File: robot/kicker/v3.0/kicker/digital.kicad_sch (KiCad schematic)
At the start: 46 parts, among them J12 Conn_01x02, J2 Conn_ARM_JTAG_SWD_10, J4 Conn_01x10, Q4 BSS138K, SW1 BTN0, SW1 RST, SW4 SW_DIP_x04, U12 AT25DF041x-UxN-x, U13 AD8494, U4 STM32F411RETx, U5 SK9822, U6 SK9822

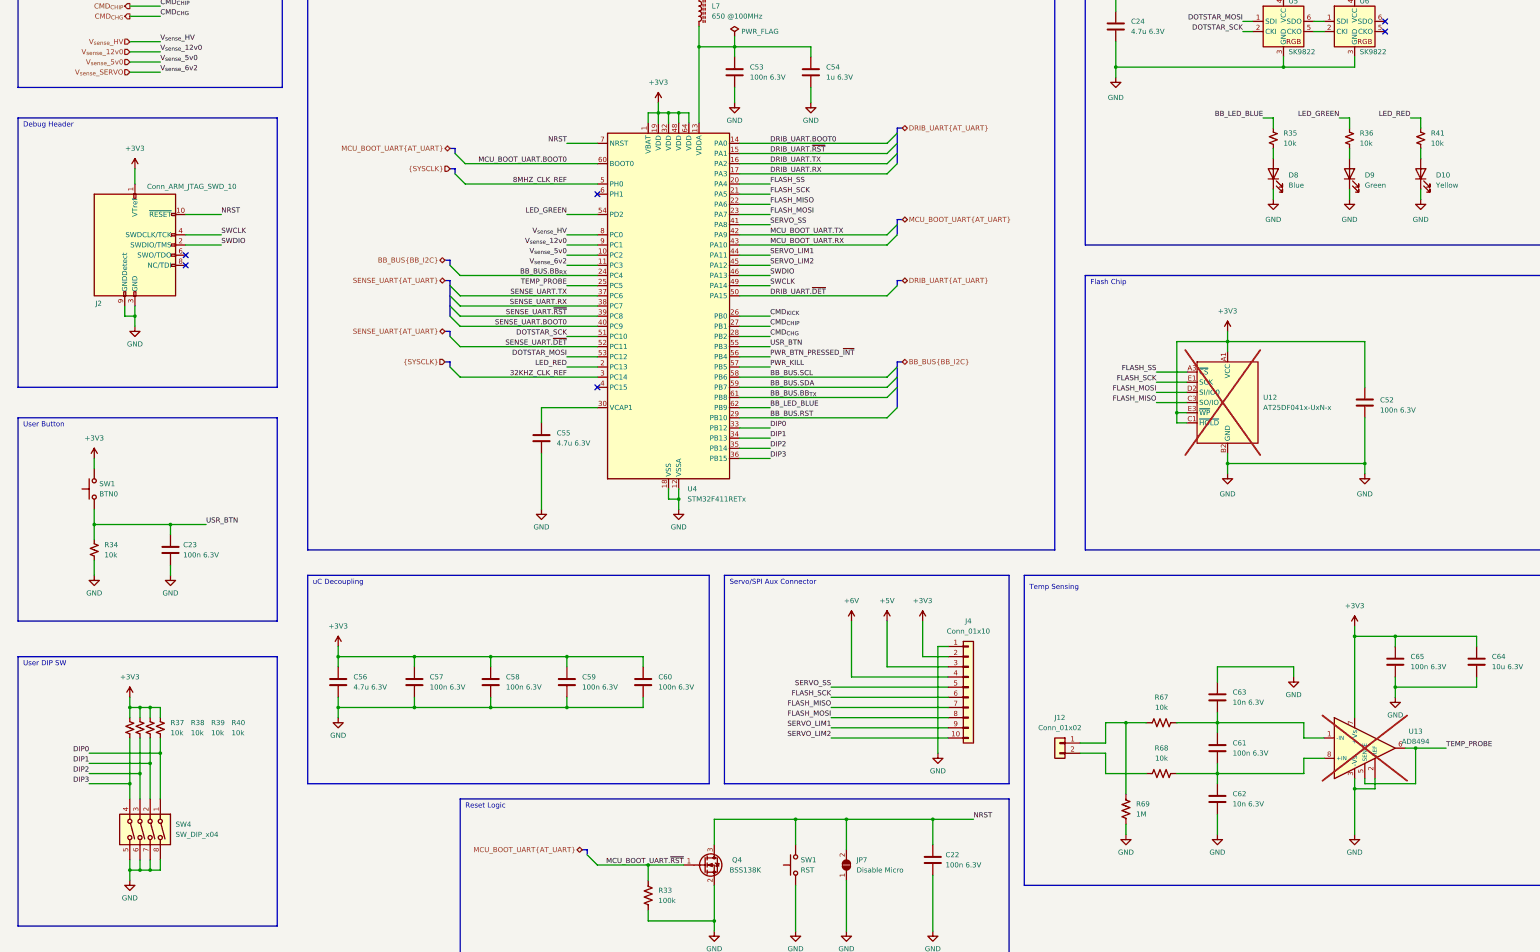
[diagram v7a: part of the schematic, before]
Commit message: kicker v3.0 changes from design review
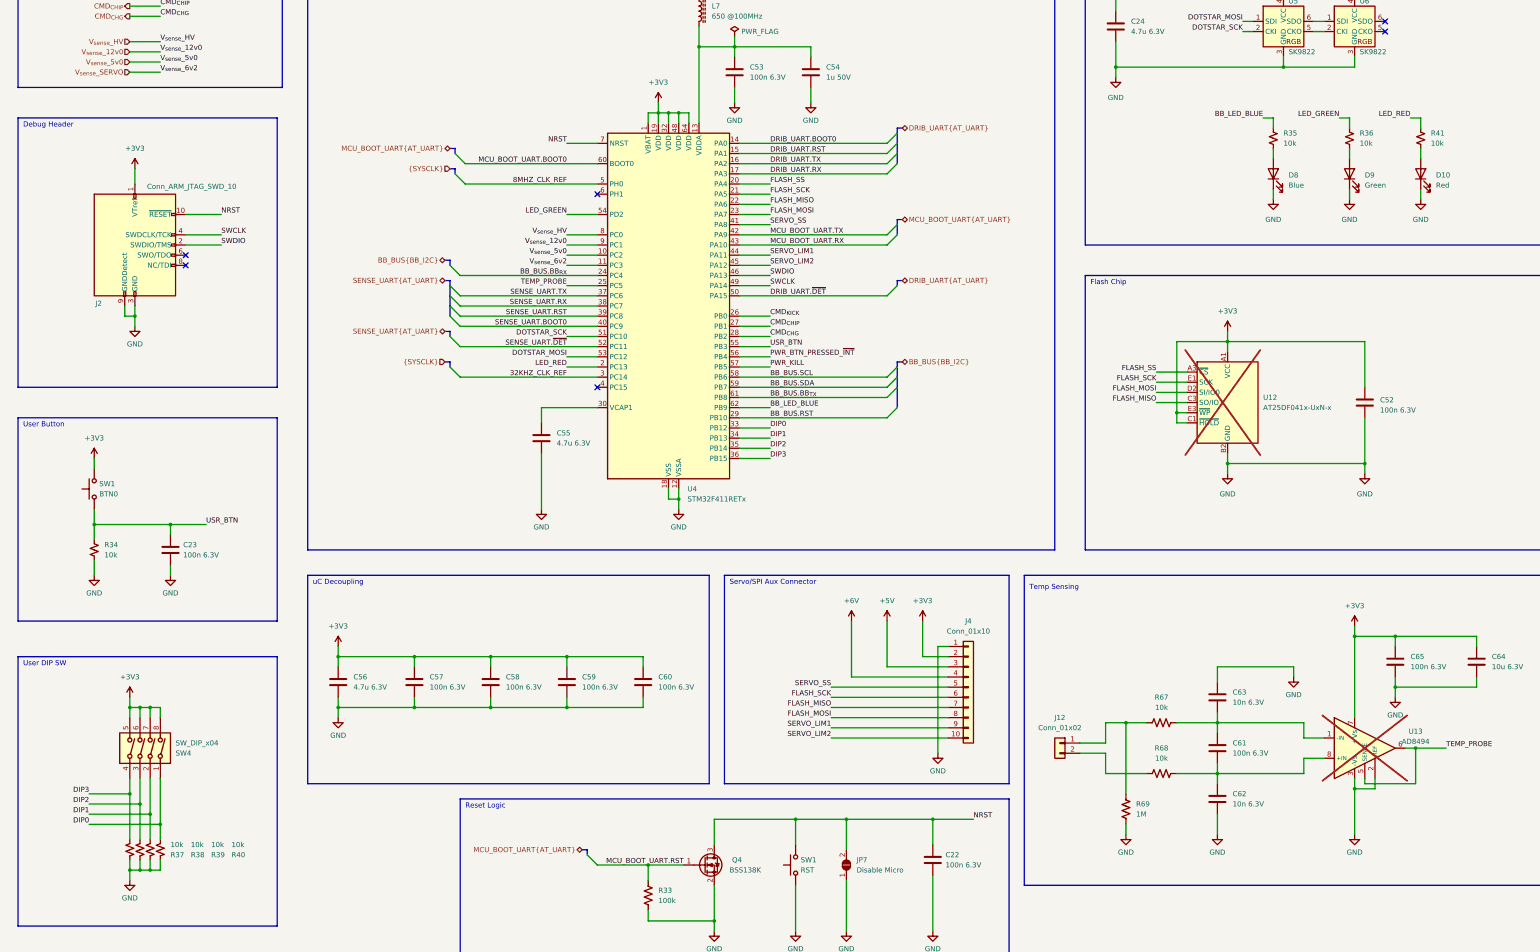
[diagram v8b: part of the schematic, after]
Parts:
- C54: value 1u 6.3V -> 1u 50V
- D10: value Yellow -> Red
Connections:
- net +3V3: now also SW4.5, SW4.6, SW4.7, SW4.8; no longer R37.1, R38.1, R39.1, R40.1
- net GND: now also R37.1, R38.1, R39.1, R40.1; no longer SW4.5, SW4.6, SW4.7, SW4.8
- net DRIB_UART.~{RST} renamed DRIB_UART.RST
- net MCU_BOOT_UART.~{RST} renamed MCU_BOOT_UART.RST
- net SENSE_UART.~{RST} renamed SENSE_UART.RST
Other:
- moved on the sheet: R37, R38, R39, R40, SW4
